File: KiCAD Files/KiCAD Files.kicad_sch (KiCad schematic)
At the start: 0 parts

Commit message: Schematic-V1
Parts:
- added C1, C2, C3, C4, C7: 2200uF, symbol Device:C_Polarized
- added C5, C6: 10uF, symbol Device:C_Polarized
- added C8, C9: 100nF, symbol Device:C
- added D1: KBPC3510W, Diode_THT:Diode_Bridge_GeneSiC_KBPC_W, symbol Diode_Bridge:KBPC3510W
- added D2, D3, D4: 1N4007, Diode_THT:D_DO-41_SOD81_P10.16mm_Horizontal, symbol Diode:1N4007
- added J1: Power-Input, symbol Connector_Generic:Conn_01x02
- added J10: SPI-Expansion, symbol Connector_Generic:Conn_01x06
- added J11: I2C-Expansion, symbol Connector_Generic:Conn_01x04
- added J2: Pump-Conn, symbol Connector_Generic:Conn_01x02
- added J3: Chopper-Conn, symbol Connector_Generic:Conn_01x02
- added J4: Heater-Conn, symbol Connector_Generic:Conn_01x02
- added J5: Term-1, symbol Connector_Generic:Conn_01x03
- added J6: Term-2, symbol Connector_Generic:Conn_01x03
- added J7: Humidity, symbol Connector_Generic:Conn_01x03
- added J8: MQ-2-Methane, symbol Connector_Generic:Conn_01x03
- added J9: MQ-135-CO2, symbol Connector_Generic:Conn_01x03
- added K2: Chopper-Relay, G2R-1-DC5:RELAY_G2R-1 AC12_OMR, symbol G2R-1-DC5:G2R-1_DC5
- added K3: Heater-Relay, G2R-1-DC5:RELAY_G2R-1 AC12_OMR, symbol G2R-1-DC5:G2R-1_DC5
- added Q1: IRFZ44N, Package_TO_SOT_THT:TO-220-3_Vertical, symbol Transistor_FET:IRF540N
- added Q2, Q3: BD139, Package_TO_SOT_THT:TO-126-3_Vertical, symbol Transistor_BJT:BD139
- added R1, R5: 100, symbol Device:R
- added R2, R3: 4.7k, symbol Device:R
- added R4, R6, R7: 10k, symbol Device:R
- added U1: Arduino_Nano_ESP32, Module:Arduino_Nano, symbol MCU_Module:Arduino_Nano_ESP32
- added U2: LM7805, Package_TO_SOT_THT:TO-220-3_Vertical, symbol Regulator_Linear:LM7805_TO220
- added U3: LM7808, Package_TO_SOT_THT:TO-220-3_Vertical, symbol Regulator_Linear:LM7808_TO220
- added U4: LM7812, Package_TO_SOT_THT:TO-220-3_Vertical, symbol Regulator_Linear:LM7812_TO220
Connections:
- new net: J3.1 (Pin_1), K2.4
- new net: J10.2 (Pin_2), U1.13 (D10/CS)
- new net: J10.3 (Pin_3), U1.14 (D11/COPI)
- new net: J10.4 (Pin_4), U1.15 (D12/CIPO)
- new net: J10.5 (Pin_5), U1.16 (D13/SCK)
- new net: C8.1, Q2.3 (B), R2.2
- new net: J8.2 (Pin_2), R4.1
- new net: C9.1, Q3.3 (B), R3.2
- new net: D3.2 (A), K2.1, Q2.2 (C)
- new net: D1.2, J1.1 (Pin_1)
- new net: D1.4, J1.2 (Pin_2)
- new net: J11.2 (Pin_2), U1.23 (SDA/A4)
- new net: J11.3 (Pin_3), U1.24 (SCL/A5)
- new net: D4.2 (A), K3.1, Q3.2 (C)
- new net: J4.2 (Pin_2), K3.3
- new net: J4.1 (Pin_1), K3.4
- new net: D2.2 (A), J2.2 (Pin_2), Q1.2 (D)
- new net: Q1.1 (G), R1.2
- new net: J9.2 (Pin_2), R5.1
- new net +12V: C7.1, K2.3, U4.3 (VO)
- new net +3.3V: J10.1 (Pin_1), J11.1 (Pin_1), J5.1 (Pin_1), J6.1 (Pin_1), J7.1 (Pin_1), U1.17 (3V3)
- new net +5V: C5.1, D3.1 (K), D4.1 (K), J8.1 (Pin_1), J9.1 (Pin_1), K2.5, K3.5, U2.3 (VO)
- new net +8V: C6.1, U1.30 (VIN), U3.3 (VO)
- new net CO2: R5.2, R7.2, U1.21 (A2)
- new net Chopper: R2.1, U1.11 (D8)
- new net GND: C1.2, C2.2, C3.2, C4.2, C5.2, C6.2, C7.2, C8.2, C9.2, D1.3 (-), J10.6 (Pin_6), J11.4 (Pin_4), J3.2 (Pin_2), J5.3 (Pin_3), J6.3 (Pin_3), J7.3 (Pin_3), J8.3 (Pin_3), J9.3 (Pin_3), Q1.3 (S), Q2.1 (E), Q3.1 (E), R6.1, R7.1, U1.29 (GND), U1.4 (GND), U2.2 (GND), U3.2 (GND), U4.2 (GND)
- new net Heater: R3.1, U1.12 (D9)
- new net Humidity: J7.2 (Pin_2), U1.19 (A0)
- new net Methane: R4.2, R6.2, U1.20 (A1)
- new net Pump: R1.1, U1.10 (D7)
- new net Term-1: J5.2 (Pin_2), U1.7 (D4)
- new net Term-2: J6.2 (Pin_2), U1.8 (D5)
- new net VS: C1.1, C2.1, C3.1, C4.1, D1.1 (+), D2.1 (K), J2.1 (Pin_1), U2.1 (VI), U3.1 (VI), U4.1 (VI)
- no-connect marks 0 -> 12

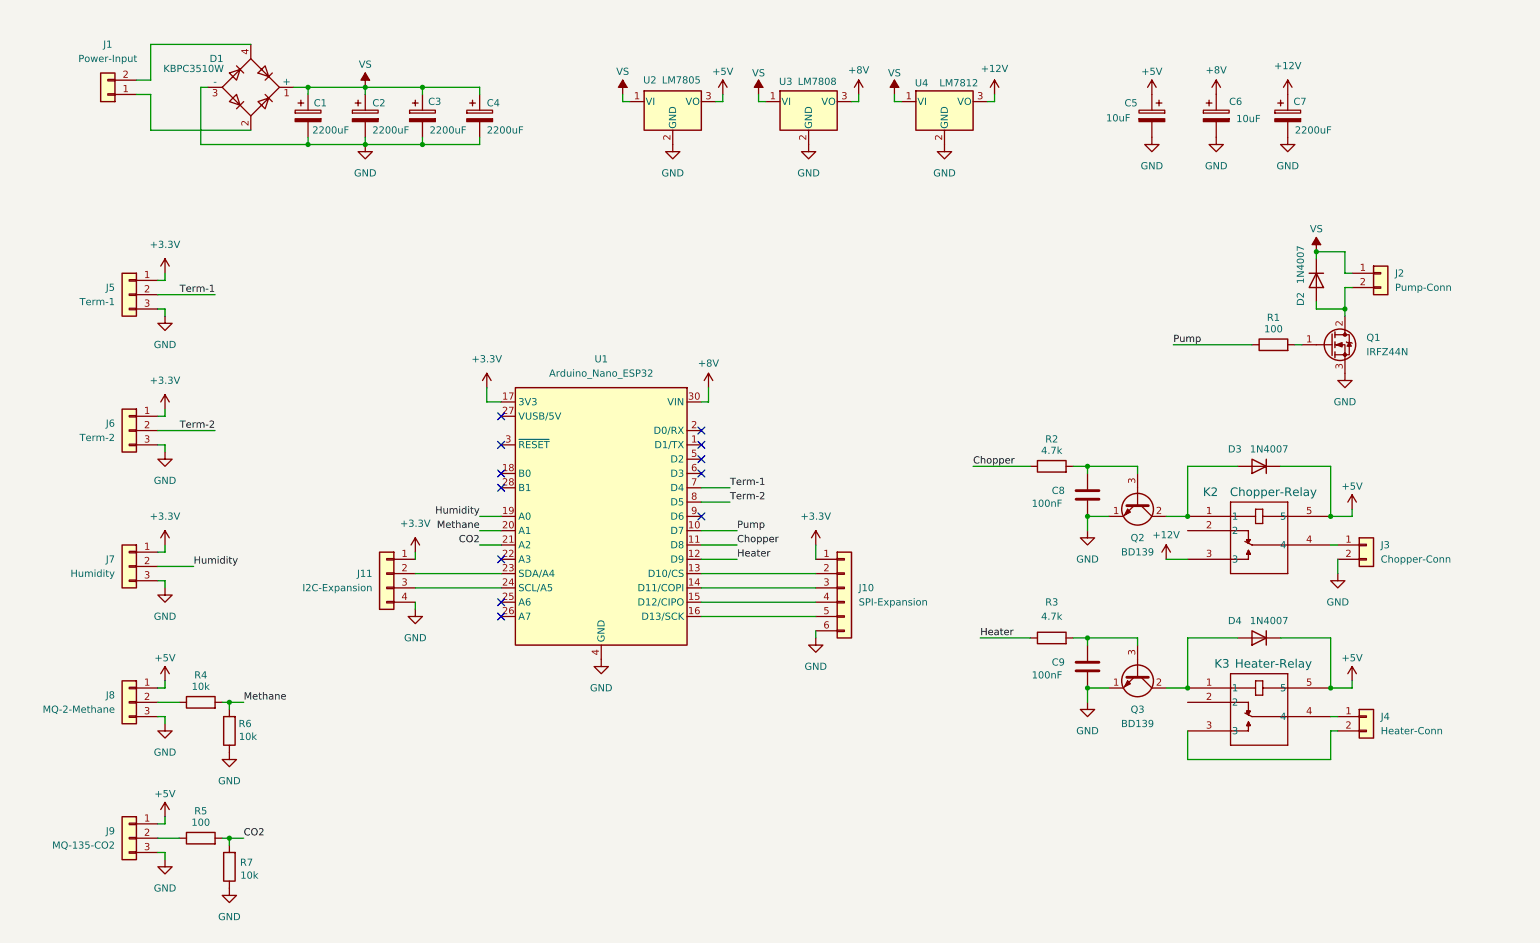
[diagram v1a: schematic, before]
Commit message: Schematic-V2-Add-Flow-Control
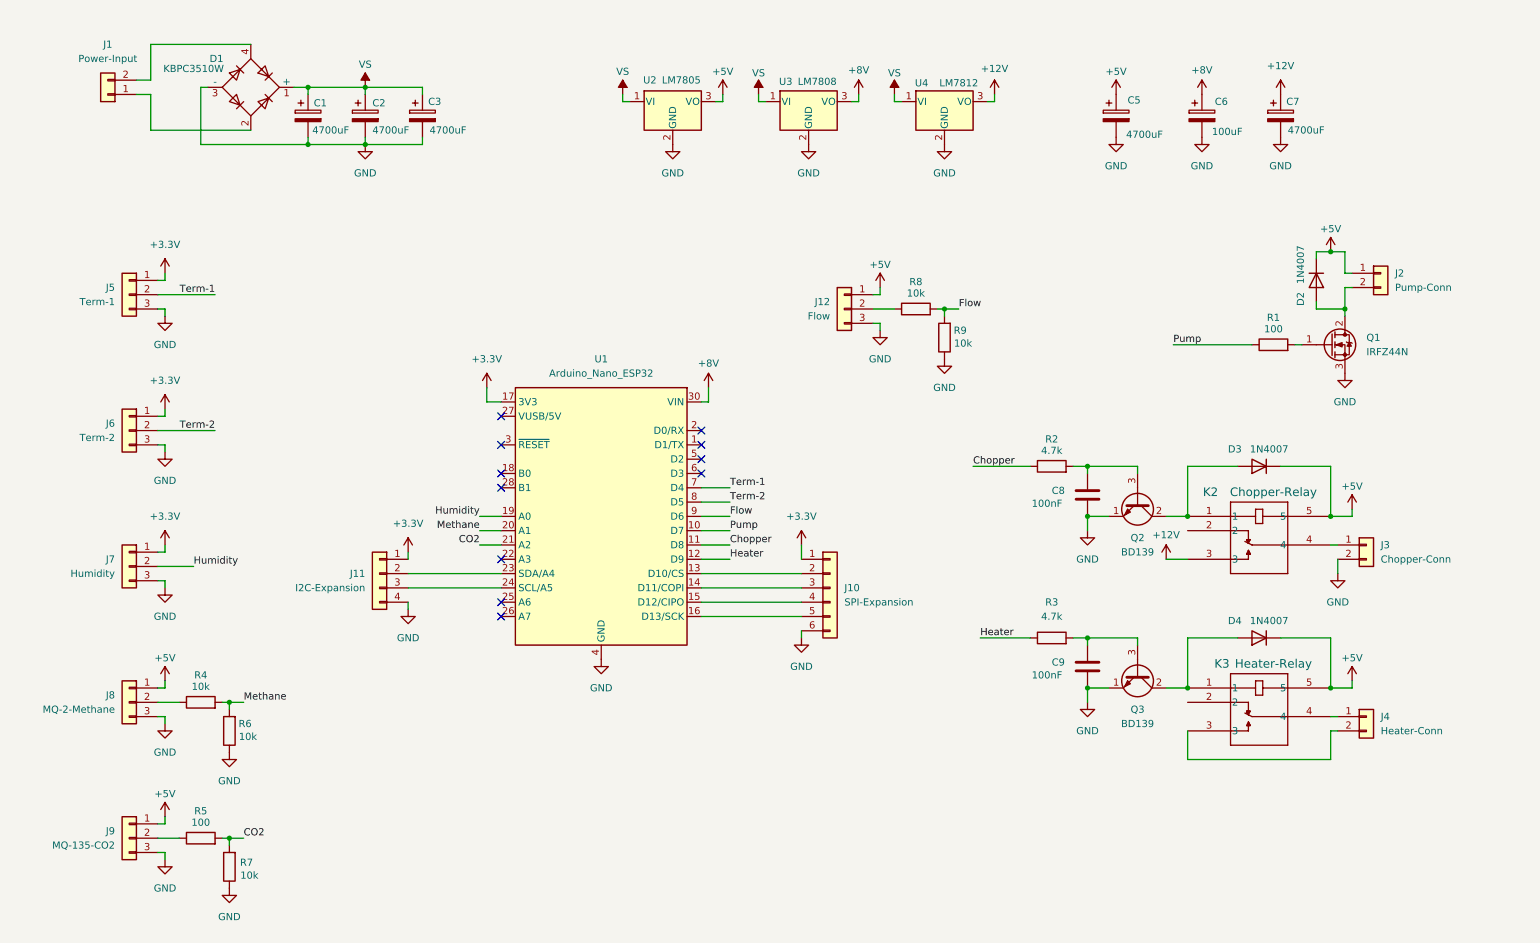
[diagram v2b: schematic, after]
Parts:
- removed C4: 2200uF, symbol Device:C_Polarized
- added J12: Flow, symbol Connector_Generic:Conn_01x03
- added R8, R9: 10k, symbol Device:R
- C1, C2, C3, C7: value 2200uF -> 4700uF
- C5: value 10uF -> 4700uF
- C6: value 10uF -> 100uF
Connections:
- net +5V: now also D2.1 (K), J2.1 (Pin_1), J12.1 (Pin_1)
- net GND: now also J12.3 (Pin_3), R9.1
- net VS: no longer D2.1 (K), J2.1 (Pin_1)
- net Flow: now reaches U1.9 (D6)
- net Flow: now also R8.2, R9.2
- new net: J12.2 (Pin_2), R8.1
- no-connect marks 12 -> 11
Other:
- moved on the sheet: C5, C6, C7, J10, J11

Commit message: Schemati-Rearranged
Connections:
- net +5V: now also J12.3 (Pin_3); no longer J12.1 (Pin_1)
- net GND: now also J12.2 (Pin_2); no longer J12.3 (Pin_3)
- net at R8.1: now also J12.1 (Pin_1); no longer J12.2 (Pin_2)
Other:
- moved on the sheet: D2, J10, J11, J12, J2, J5, J6, J7, J8, J9, Q1, R1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

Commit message: Schematic-Footprints+LEDs
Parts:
- removed J1: Power-Input, symbol Connector_Generic:Conn_01x02
- added D5, D6, D7: LED, LED_THT:LED_D5.0mm, symbol Device:LED
- added J1: Power-Input, Connector_Phoenix_MC_HighVoltage:PhoenixContact_MCV_1,5_3-G-5.08_1x03_P5.08mm_Vertical, symbol Connector_Generic:Conn_01x03
- added R11, R12, R13: 100, Resistor_THT:R_Axial_DIN0207_L6.3mm_D2.5mm_P10.16mm_Horizontal, symbol Device:R
- added R2: 10K, Resistor_THT:R_Axial_DIN0207_L6.3mm_D2.5mm_P10.16mm_Horizontal, symbol Device:R
- C1, C2, C3, C5, C7: footprint (none) -> Capacitor_THT:CP_Radial_D16.0mm_P7.50mm
- C6, R1: footprint (none) -> Resistor_THT:R_Axial_DIN0207_L6.3mm_D2.5mm_P10.16mm_Horizontal
- C8, C9: footprint (none) -> Capacitor_THT:C_Disc_D9.0mm_W2.5mm_P5.00mm
- J10: footprint (none) -> Connector_JST:JST_EH_B6B-EH-A_1x06_P2.50mm_Vertical
- J11: footprint (none) -> Connector_JST:JST_EH_B4B-EH-A_1x04_P2.50mm_Vertical
- J12, J5, J6, J7, J8, J9: footprint (none) -> Connector_JST:JST_EH_B3B-EH-A_1x03_P2.50mm_Vertical
- J2, J3, J4: footprint (none) -> Connector_Phoenix_MC_HighVoltage:PhoenixContact_MCV_1,5_2-G-5.08_1x02_P5.08mm_Vertical
- R10: renamed from R9; value 10k -> 20K; footprint (none) -> Resistor_THT:R_Axial_DIN0207_L6.3mm_D2.5mm_P10.16mm_Horizontal
- R3: renamed from R2; value 4.7k -> 220; footprint (none) -> Resistor_THT:R_Axial_DIN0207_L6.3mm_D2.5mm_P10.16mm_Horizontal
- R4: renamed from R3; value 4.7k -> 220; footprint (none) -> Resistor_THT:R_Axial_DIN0207_L6.3mm_D2.5mm_P10.16mm_Horizontal
- R5: value 100 -> 10K; footprint (none) -> Resistor_THT:R_Axial_DIN0207_L6.3mm_D2.5mm_P10.16mm_Horizontal
- R6: renamed from R7; value 10k -> 20K; footprint (none) -> Resistor_THT:R_Axial_DIN0207_L6.3mm_D2.5mm_P10.16mm_Horizontal
- R7: renamed from R4; value 10k -> 10K; footprint (none) -> Resistor_THT:R_Axial_DIN0207_L6.3mm_D2.5mm_P10.16mm_Horizontal
- R8: renamed from R6; value 10k -> 20K; footprint (none) -> Resistor_THT:R_Axial_DIN0207_L6.3mm_D2.5mm_P10.16mm_Horizontal
- R9: renamed from R8; value 10k -> 10K; footprint (none) -> Resistor_THT:R_Axial_DIN0207_L6.3mm_D2.5mm_P10.16mm_Horizontal
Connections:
- net +5V: now also D7.2 (A), R11.2, R12.2
- net GND: now also R2.2
- net at D3.2 (A), K2.1, Q2.2 (C): now also D5.1 (K)
- net at D1.2: now also J1.3 (Pin_3)
- net at D1.4: now also J1.1 (Pin_1)
- net at D4.2 (A), K3.1, Q3.2 (C): now also D6.1 (K)
- net at D2.2 (A), J2.2 (Pin_2), Q1.2 (D): now also R13.2
- net at Q1.1 (G), R1.2: now also R2.1
- new net: D5.2 (A), R11.1
- new net: D6.2 (A), R12.1
- new net: D7.1 (K), R13.1
- no-connect marks 11 -> 14
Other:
- moved on the sheet: C1, C2, C3, C5, C6, C7, C8, D1, D2, D3, J2, J3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

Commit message: Layout-Designed
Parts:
- C6: footprint Resistor_THT:R_Axial_DIN0207_L6.3mm_D2.5mm_P10.16mm_Horizontal -> Capacitor_THT:CP_Radial_D8.0mm_P3.80mm
- J10: footprint Connector_JST:JST_EH_B6B-EH-A_1x06_P2.50mm_Vertical -> Connector_JST:JST_XH_B6B-XH-A_1x06_P2.50mm_Vertical
- J11: footprint Connector_JST:JST_EH_B4B-EH-A_1x04_P2.50mm_Vertical -> Connector_JST:JST_XH_B4B-XH-A_1x04_P2.50mm_Vertical
- J12, J5, J6, J7, J8, J9: footprint Connector_JST:JST_EH_B3B-EH-A_1x03_P2.50mm_Vertical -> Connector_JST:JST_XH_B3B-XH-A_1x03_P2.50mm_Vertical
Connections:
- net +3.3V: now also J11.4 (Pin_4); no longer J11.1 (Pin_1)
- net GND: now also J11.1 (Pin_1), J5.2 (Pin_2), J6.2 (Pin_2), J7.2 (Pin_2); no longer J11.4 (Pin_4), J5.3 (Pin_3), J6.3 (Pin_3), J7.3 (Pin_3)
- net Humidity: now also J7.3 (Pin_3); no longer J7.2 (Pin_2)
- net Term-1: now also J5.3 (Pin_3); no longer J5.2 (Pin_2)
- net Term-2: now also J6.3 (Pin_3); no longer J6.2 (Pin_2)
- net at J11.2 (Pin_2): now also U1.24 (SCL/A5); no longer U1.23 (SDA/A4)
- net at J11.3 (Pin_3): now also U1.23 (SDA/A4); no longer U1.24 (SCL/A5)
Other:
- moved on the sheet: J11

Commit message: Redesigned&Fixed-Final-PCB
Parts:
- removed C8, C9: 100nF, Capacitor_THT:C_Disc_D9.0mm_W2.5mm_P5.00mm, symbol Device:C
- removed J10: SPI-Expansion, Connector_JST:JST_XH_B6B-XH-A_1x06_P2.50mm_Vertical, symbol Connector_Generic:Conn_01x06
- removed J11: I2C-Expansion, Connector_JST:JST_XH_B4B-XH-A_1x04_P2.50mm_Vertical, symbol Connector_Generic:Conn_01x04
- added C4: 100nF, symbol Device:C
- added Q4, Q5: IRFZ44N, Package_TO_SOT_THT:TO-220-3_Vertical, symbol Transistor_FET:IRF540N
- added R14: 22K, Resistor_THT:R_Axial_DIN0207_L6.3mm_D2.5mm_P10.16mm_Horizontal, symbol Device:R
- added R15: 1.1K, Resistor_THT:R_Axial_DIN0207_L6.3mm_D2.5mm_P10.16mm_Horizontal, symbol Device:R
- added R16, R17: 4.7K, Resistor_THT:R_Axial_DIN0207_L6.3mm_D2.5mm_P10.16mm_Horizontal, symbol Device:R
- R3: value 220 -> 1.1K
- R4: value 220 -> 22K
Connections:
- net +3.3V: now also R16.1, R17.1
- net +5V: now also R3.2, R15.2
- net +8V: now also C4.1
- net Chopper: now also R14.1; no longer R3.1
- net GND: now also C4.2, Q4.3 (S), Q5.3 (S)
- net Term-1: now also R16.2
- net Term-2: now also R17.2
- net at D3.2 (A), D5.1 (K), K2.1: now also Q4.2 (D); no longer Q2.2 (C)
- net at Q2.3 (B): now also R14.2; no longer R3.2
- net at D4.2 (A), D6.1 (K), K3.1: now also Q5.2 (D); no longer Q3.2 (C)
- new net: Q2.2 (C), Q4.1 (G), R3.1
- new net: Q3.2 (C), Q5.1 (G), R15.1
- no-connect marks 14 -> 20
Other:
- moved on the sheet: C5, C6, C7, D2, D3, D4, D5, D6, D7, J2, J3, J4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
